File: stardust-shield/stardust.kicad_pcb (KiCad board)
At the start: 2 copper layers, 154.3 x 139.1 mm, 17 parts, among them J1 BEXUS 28V, J2 Pololu J8557, J3 Pololu J9251, J4 DS3231M, U1 IRFL210, U2 IRFL210, U5 DS18B20, U6 DS18B20, U8 DHT22, U9 SSCDRNN015PASA5

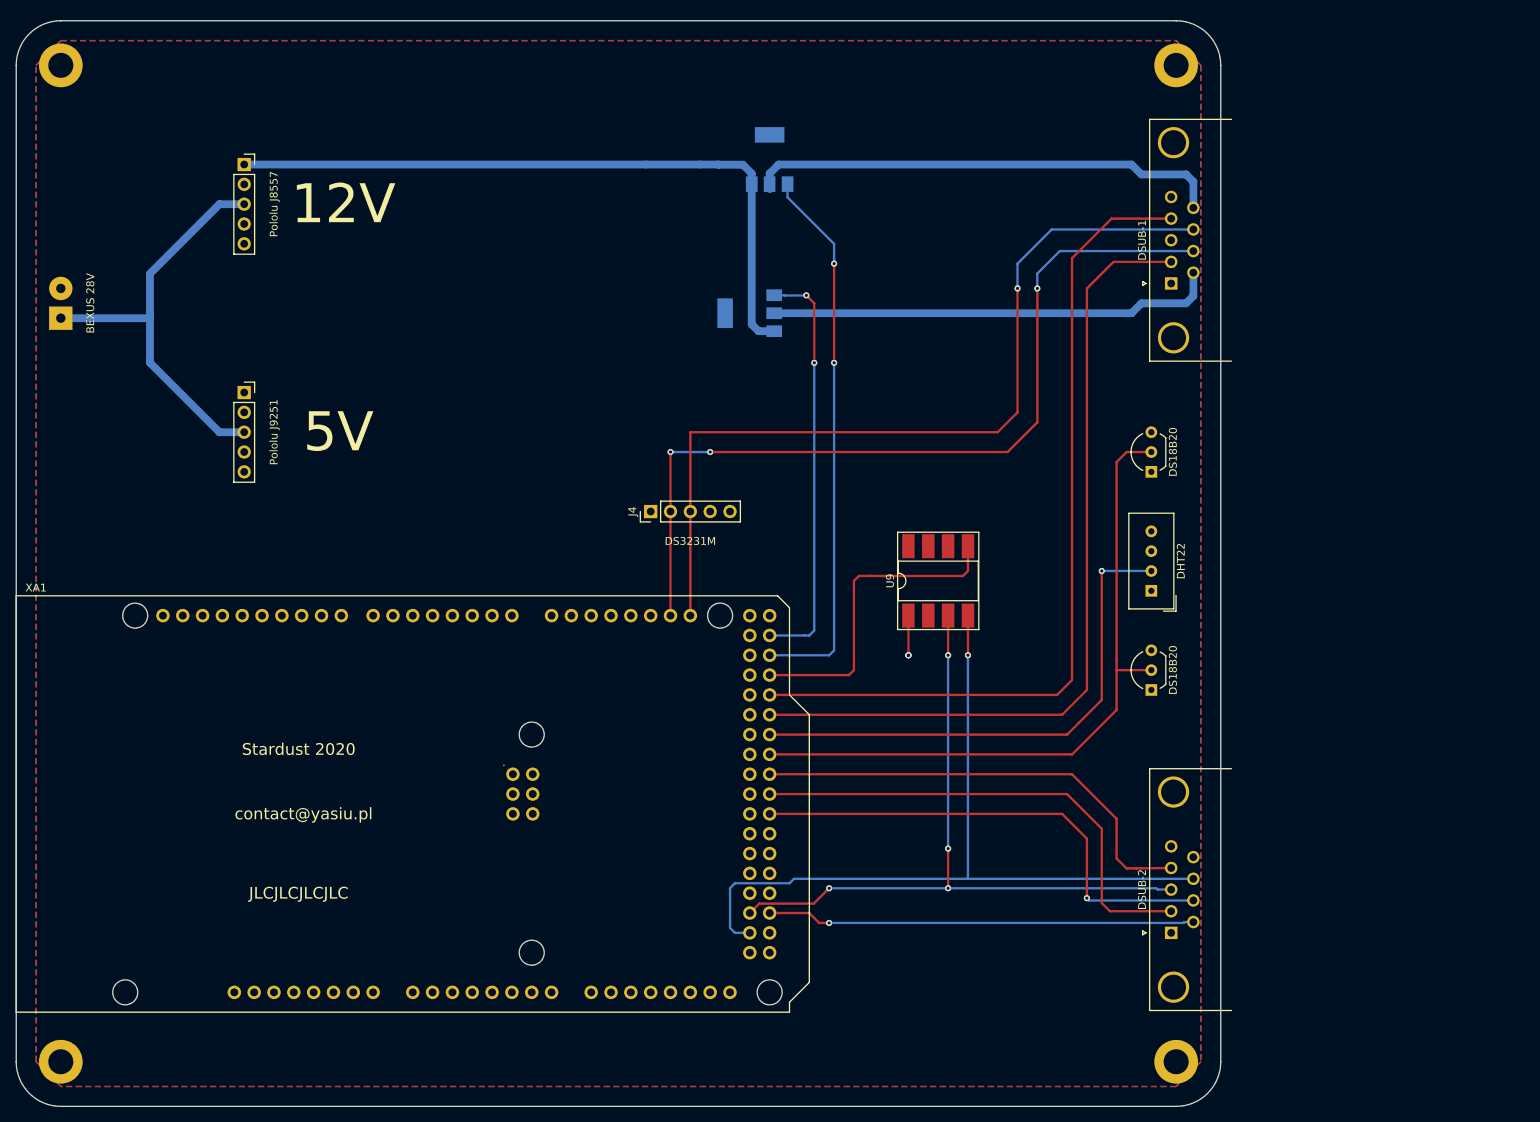
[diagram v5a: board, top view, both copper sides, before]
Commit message: move mosfet to mech board, controll pump via gnd
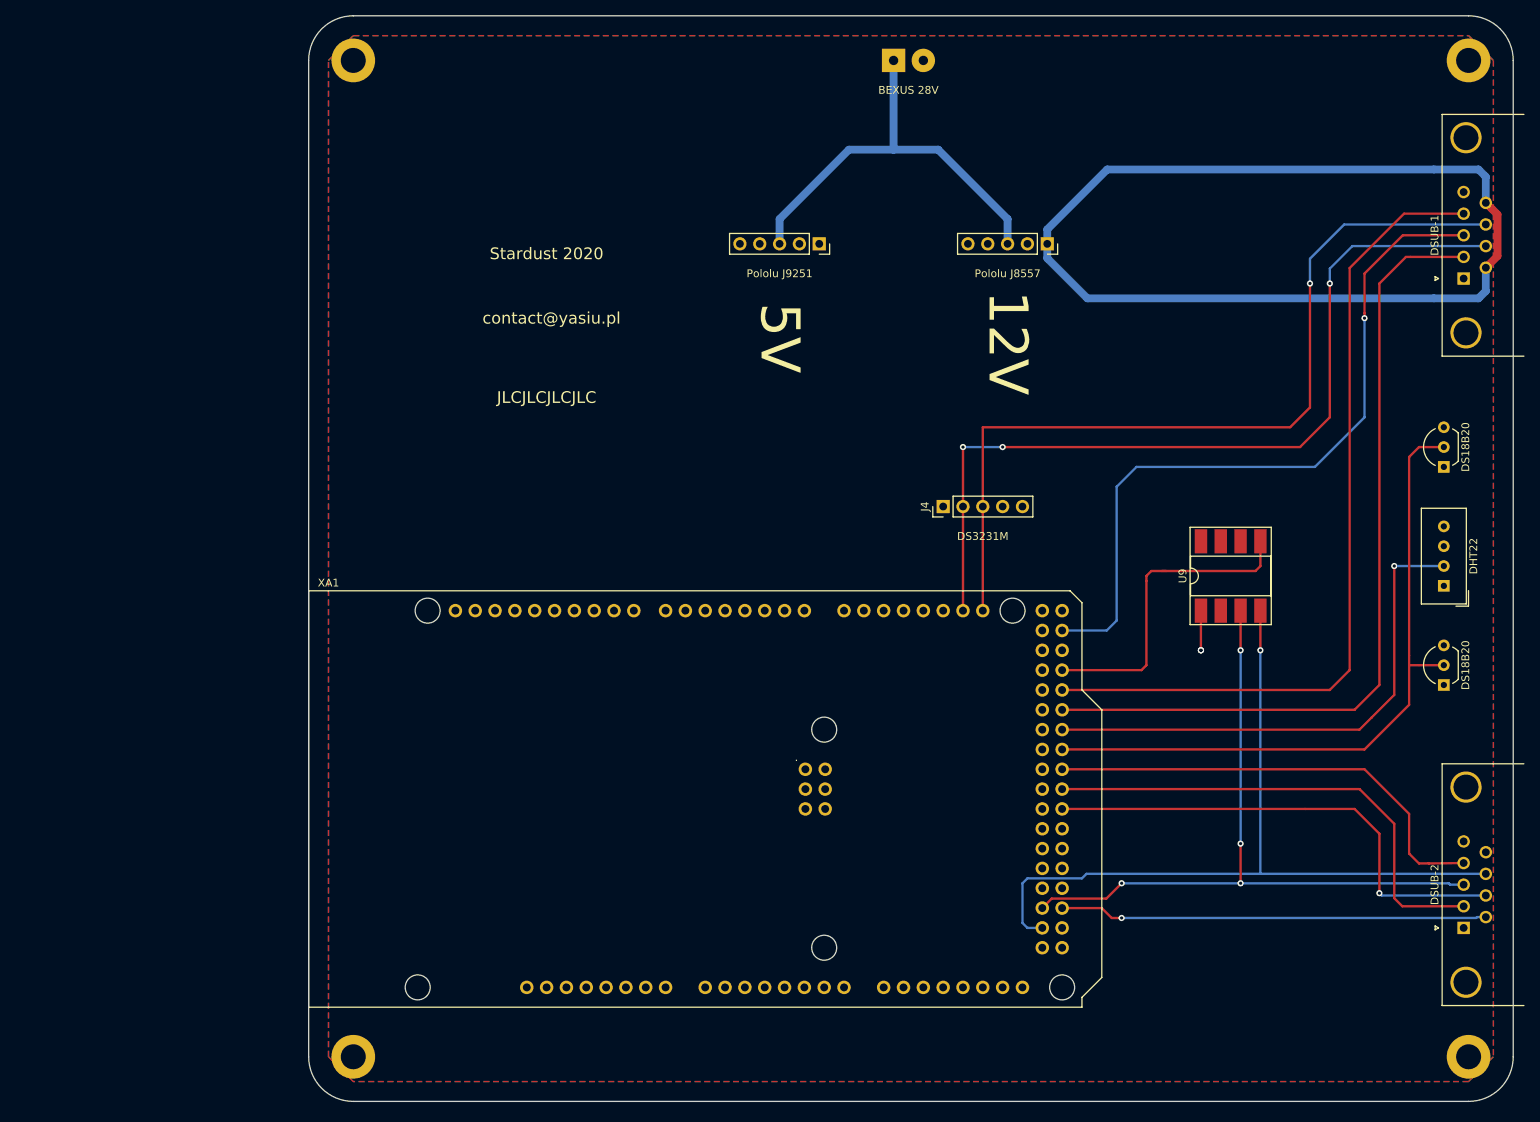
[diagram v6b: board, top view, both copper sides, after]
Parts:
- removed the REF** at (51.4, 151.8)
- removed the REF** at (194.3, 151.8)
- removed the REF** at (51.4, 24.1)
- removed U1, U2: IRFL210, Package_TO_SOT_SMD:SOT-223
- added REF**: MountingHole_3.2mm_M3_DIN965_Pad, MountingHole:MountingHole_3.2mm_M3_DIN965_Pad, F.Cu at (88.9, 151.1)
- added REF**: MountingHole_3.2mm_M3_DIN965_Pad, MountingHole:MountingHole_3.2mm_M3_DIN965_Pad, F.Cu at (231.8, 151.1)
- added REF**: MountingHole_3.2mm_M3_DIN965_Pad, MountingHole:MountingHole_3.2mm_M3_DIN965_Pad, F.Cu at (88.9, 23.5)
- moved J1 111.7 mm to (158.1, 23.5), turned to 0 degrees
- moved J2 103.4 mm to (177.8, 47.0), turned to 270 degrees
- moved J3 76.1 mm to (148.6, 47.0), turned to 270 degrees
- moved J4 37.5 mm to (164.5, 80.6)
- moved REF** 37.5 mm to (231.8, 23.5)
- moved U5 37.5 mm to (228.6, 75.6)
- moved U6 37.5 mm to (228.6, 103.5)
- moved U8 37.5 mm to (228.6, 90.8)
- moved XA1 37.5 mm to (83.2, 144.8)
- moved DSUB-1 37.5 mm to (231.1, 51.4)
- moved DSUB-2 37.5 mm to (231.1, 134.6)
- moved U9 37.5 mm to (201.3, 89.5)
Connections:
- DSUB-1 pad 3: Net-(DSUB-1-Pad3) -> Pump-GPIO
- DSUB-1 pad 6: Pump-2 -> +12V
- DSUB-1 pad 9: Pump-1 -> +12V
- XA1 pad D23: Pump-GPIO-2 -> Pump-GPIO
- XA1 pad D25: Pump-GPIO-1 -> Net-(XA1-PadD25)
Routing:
- net Pump-GPIO: track 0.00 -> 93.2 mm, vias 0 -> 1
- net Pump-GPIO-1: track 70.7 -> 0.00 mm, vias 2 -> 0
- net Pump-1: track 61.0 -> 0.00 mm
- net Pump-2: track 57.6 -> 0.00 mm
- net Pump-GPIO-2: track 53.4 -> 0.00 mm, vias 2 -> 0
- net +12V: track 88.7 -> 138.0 mm
- net DHT22-1: track 108.4 -> 106.9 mm

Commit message: update fill area
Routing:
- net +12V: track 138.0 -> 74.5 mm
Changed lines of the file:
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@@
     (thickness 1.6)
     (drawings 14)
-    (tracks 163)
+    (tracks 157)
     (zones 0)
     (modules 15)
@@
   )
   (setup
-    (last_trace_width 0.3)
+    (last_trace_width 1)
     (user_trace_width 0.3)
     (user_trace_width 0.5)
@@
     )
   )
-  (gr_text 5V (at 143.51 59.055 270) (layer F.SilkS)
+  (gr_text 5V (at 143.51 56.515) (layer F.SilkS)
     (effects (font (size 5 5) (thickness 0.3)))
   )
-  (gr_text 12V (at 172.72 59.69 270) (layer F.SilkS)
+  (gr_text 12V (at 172.72 56.515) (layer F.SilkS)
     (effects (font (size 5 5) (thickness 0.3)))
   )
@@
   (via (at 213.995 52.07) (size 0.8) (drill 0.4) (layers F.Cu B.Cu) (net 3))
   (segment (start 172.085 73.025) (end 167.005 73.025) (width 0.3) (layer B.Cu) (net 3))
-  (segment (start 233.98 53.04) (end 233.98 50.05) (width 1) (layer B.Cu) (net 10))
-  (segment (start 233.045 53.975) (end 233.98 53.04) (width 1) (layer B.Cu) (net 10))
-  (segment (start 227.33 53.975) (end 233.045 53.975) (width 1) (layer B.Cu) (net 10))
   (segment (start 231.14 43.125) (end 223.50288 43.125) (width 0.3) (layer F.Cu) (net 5))
   (segment (start 223.50288 43.125) (end 216.535 50.09288) (width 0.3) (layer F.Cu) (net 5))
@@
   (segment (start 223.29 131.85) (end 222.25 130.81) (width 0.3) (layer F.Cu) (net 9))
   (segment (start 222.25 130.81) (end 222.25 121.285) (width 0.3) (layer F.Cu) (net 9))
-  (segment (start 234.779999 42.539999) (end 233.98 41.74) (width 1) (layer F.Cu) (net 10))
-  (segment (start 235.480001 43.240001) (end 234.779999 42.539999) (width 1) (layer F.Cu) (net 10))
-  (segment (start 235.480001 48.549999) (end 235.480001 43.240001) (width 1) (layer F.Cu) (net 10))
-  (segment (start 233.98 50.05) (end 235.480001 48.549999) (width 1) (layer F.Cu) (net 10))
   (segment (start 177.8 45.14) (end 177.8 46.99) (width 1) (layer B.Cu) (net 10))
   (segment (start 185.475 37.465) (end 177.8 45.14) (width 1) (layer B.Cu) (net 10))
   (segment (start 227.33 37.465) (end 185.475 37.465) (width 1) (layer B.Cu) (net 10))
-  (segment (start 177.8 48.84) (end 177.8 46.99) (width 1) (layer B.Cu) (net 10))
-  (segment (start 182.935 53.975) (end 177.8 48.84) (width 1) (layer B.Cu) (net 10))
-  (segment (start 227.33 53.975) (end 182.935 53.975) (width 1) (layer B.Cu) (net 10))
+  (segment (start 234.779999 49.250001) (end 233.98 50.05) (width 1) (layer B.Cu) (net 10))
+  (segment (start 235.480001 48.549999) (end 234.779999 49.250001) (width 1) (layer B.Cu) (net 10))
+  (segment (start 235.480001 43.240001) (end 235.480001 48.549999) (width 1) (layer B.Cu) (net 10))
+  (segment (start 233.98 41.74) (end 235.480001 43.240001) (width 1) (layer B.Cu) (net 10))
   (segment (start 217.805 109.22) (end 179.705 109.22) (width 0.3) (layer F.Cu) (net 12))
   (segment (start 222.25 104.775) (end 222.25 88.265) (width 0.3) (layer F.Cu) (net 12))

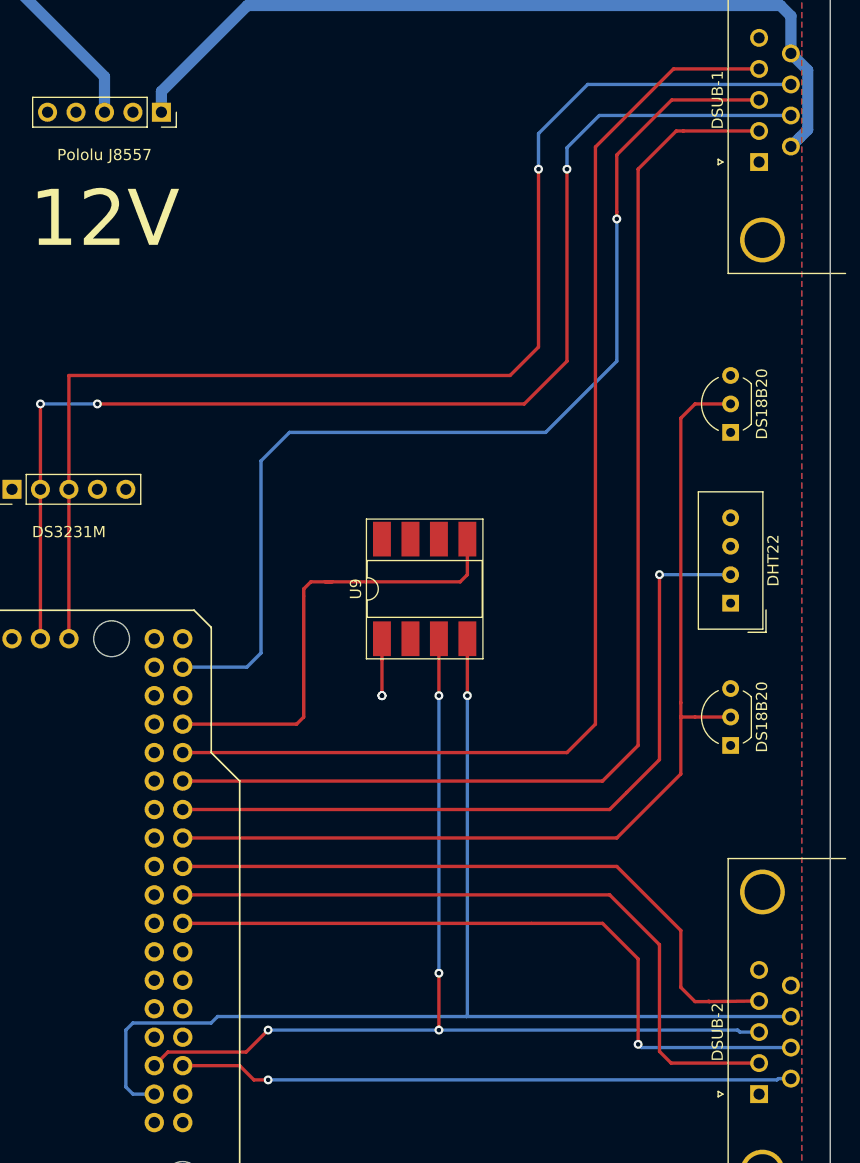
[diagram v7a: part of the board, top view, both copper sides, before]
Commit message: add pump pull-down, clean up paths
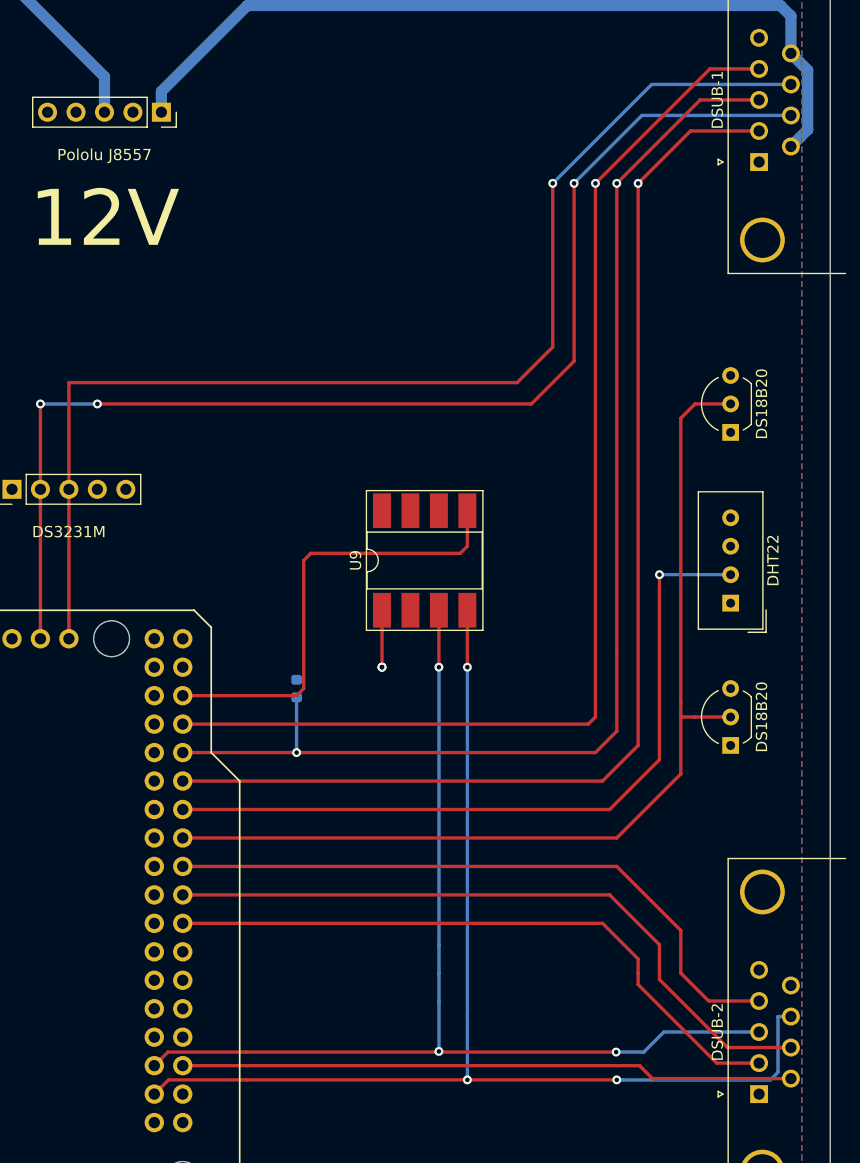
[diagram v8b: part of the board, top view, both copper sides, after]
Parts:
- added R1: 10k, Resistor_SMD:R_0603_1608Metric, B.Cu at (189.9, 98.4)
- moved U9 2.54 mm to (201.3, 87.0)
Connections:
- XA1 pad D23: Pump-GPIO -> Net-(XA1-PadD23)
- XA1 pad D25: Net-(XA1-PadD25) -> SPI-SS-Pressure-2
- XA1 pad D27: SPI-SS-Pressure-2 -> DHT22-1
- XA1 pad D29: DHT22-1 -> Pump-GPIO
- XA1 pad D39: DHT22-2 -> SPI-SS-Pressure-1
- XA1 pad D41: SPI-SS-Pressure-1 -> DHT22-2
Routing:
- net Pump-GPIO: track 93.2 -> 109.1 mm, vias 1 -> 2
- net DHT22-2: track 63.2 -> 57.9 mm
- net SPI-MISO: track 90.5 -> 94.6 mm, vias 4 -> 3
- net DHT22-1: track 106.9 -> 103.6 mm, vias 0 -> 1
- net SPI-CLK: track 101.5 -> 104.5 mm, vias 1 -> 3
- net I2C-SCL: track 109.8 -> 106.9 mm
- net I2C-SDA: track 109.8 -> 107.9 mm
- net SPI-SS-Pressure-1: track 63.3 -> 61.7 mm, vias 1 -> 0
- net 1Wire-2: track 59.5 -> 58.6 mm
- net 1Wire-1: track 105.6 -> 104.9 mm, vias 0 -> 1
- net SPI-SS-Pressure-2: track 41.4 -> 40.8 mm
- net SPI-MOSI: vias 1 -> 0
